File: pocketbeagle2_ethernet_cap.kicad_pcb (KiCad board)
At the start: 4 copper layers, 35.3 x 55.3 mm, 84 parts, among them J1 RJ45_1840888-1, J2 Header_18x02_2.54mm_2.54mm_St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, J3 Header_18x02_2.54mm_2.54mm_St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, Q1 BSS138LT1G, Q2 BSS138LT1G, Q3 BSS138LT1G, U1 PocketBeagle2, U2 DP83867IRPAPR, U3 TPS7A2011PDBVR, U4 TPS7A2025PDBVR, Y1 25M

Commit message: Switch BOM to in-stock LCSC parts, U3 to TLV73311
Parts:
- U3: value TPS7A2011PDBVR -> TLV73311PDBVR
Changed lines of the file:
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@@
 			)
 		)
-		(property "Value" "TPS7A2011PDBVR"
+		(property "Value" "TLV73311PDBVR"
 			(at 0 2.4 0)
 			(unlocked yes)

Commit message: Move LED drivers, pull-ups, TD0/TD2 resistors to top side
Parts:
- Q1, Q2, Q3, R10, R20, R21, R24, R31, R32, R8: moved to F.Cu
- moved Q1 14.2 mm to (202.2, 62.3)
- moved Q2 7.94 mm to (198.7, 62.3)
- moved Q3 4.77 mm to (195.2, 62.3)
- moved R24 3.63 mm to (190.3, 65.3), turned to 180 degrees
- moved R31 2.53 mm to (188.0, 91.2)
- moved R8 2.41 mm to (190.3, 63.9)
- moved R32 2.00 mm to (188.0, 90.0), turned to 0 degrees
- moved R10 0.90 mm to (205.2, 70.0)
- moved R20 0.80 mm to (205.2, 61.1)
- moved R21 0.80 mm to (205.2, 63.7)
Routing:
- net Net-(D1-K): track 2.63 -> 21.6 mm, vias 1 -> 2
- net /network/phy/LED0_PHY_to_Q1: track 59.5 -> 71.4 mm
- net Net-(D2-K): track 2.55 -> 13.3 mm, vias 1 -> 2
- net /VDD_3V3: track 178.7 -> 187.9 mm, vias 10 -> 11
- net /network/phy/LED1_PHY_to_Q2: track 55.7 -> 61.4 mm, vias 1 -> 2
- net Net-(U2-TX_D0): track 65.6 -> 60.1 mm, vias 1 -> 2
- net /INT_PWDN_N_CPU_PHY: track 27.2 -> 30.7 mm, vias 0 -> 1
- net /RGMII_TD0_CPU_to_PHY: track 2.26 -> 4.78 mm, vias 0 -> 1
- net GND: track 53.8 -> 56.3 mm, vias 101 -> 96
- net Net-(D3-K): track 2.55 -> 5.02 mm, vias 1 -> 2
- net Net-(U2-TX_D2): track 73.5 -> 71.2 mm, vias 1 -> 2
- net /network/phy/LED2_PHY_to_Q3: track 54.2 -> 52.8 mm, vias 1 -> 2
- net /RGMII_TD2_CPU_to_PHY: track 4.45 -> 5.35 mm
- net /MDIO_MDC_CPU_PHY: track 42.1 -> 42.9 mm
- net /MDIO_DIO_CPU_PHY: track 36.1 -> 36.9 mm

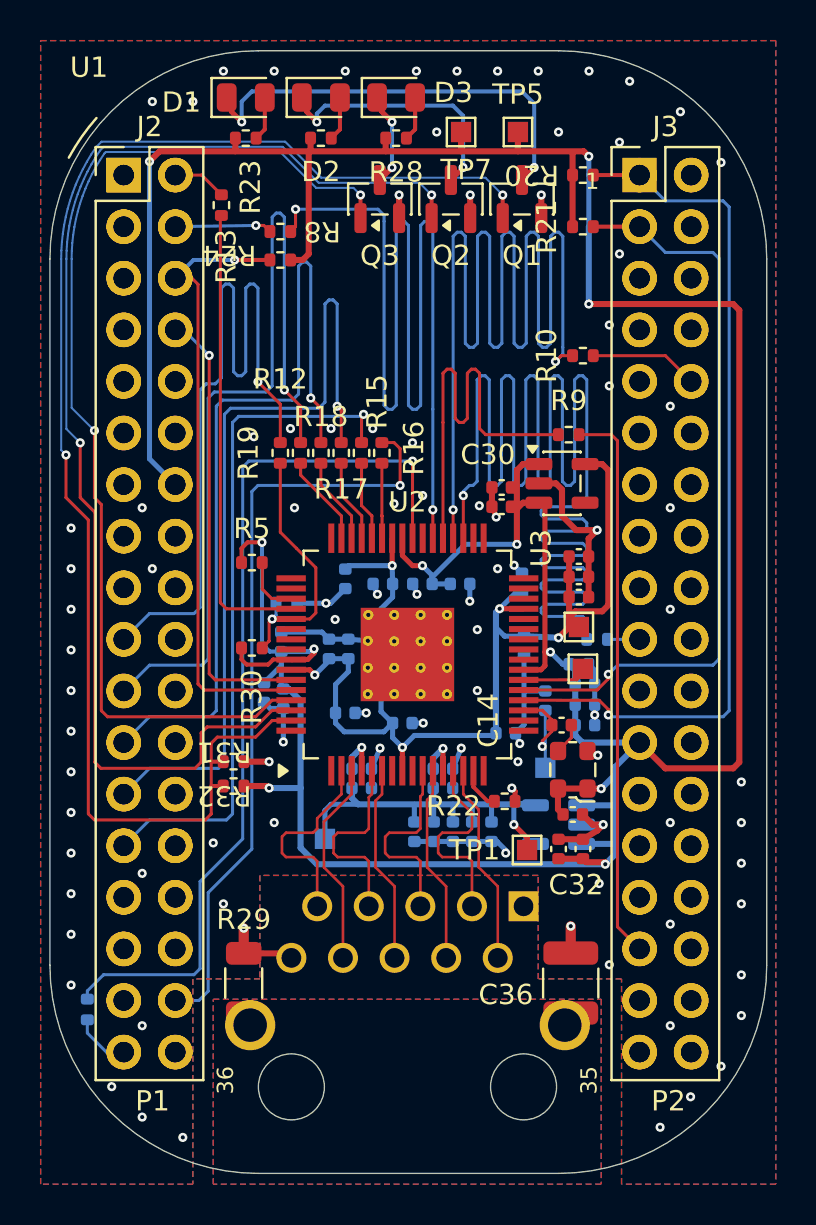
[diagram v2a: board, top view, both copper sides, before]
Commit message: Move LDO, decoupling and series resistors to top side
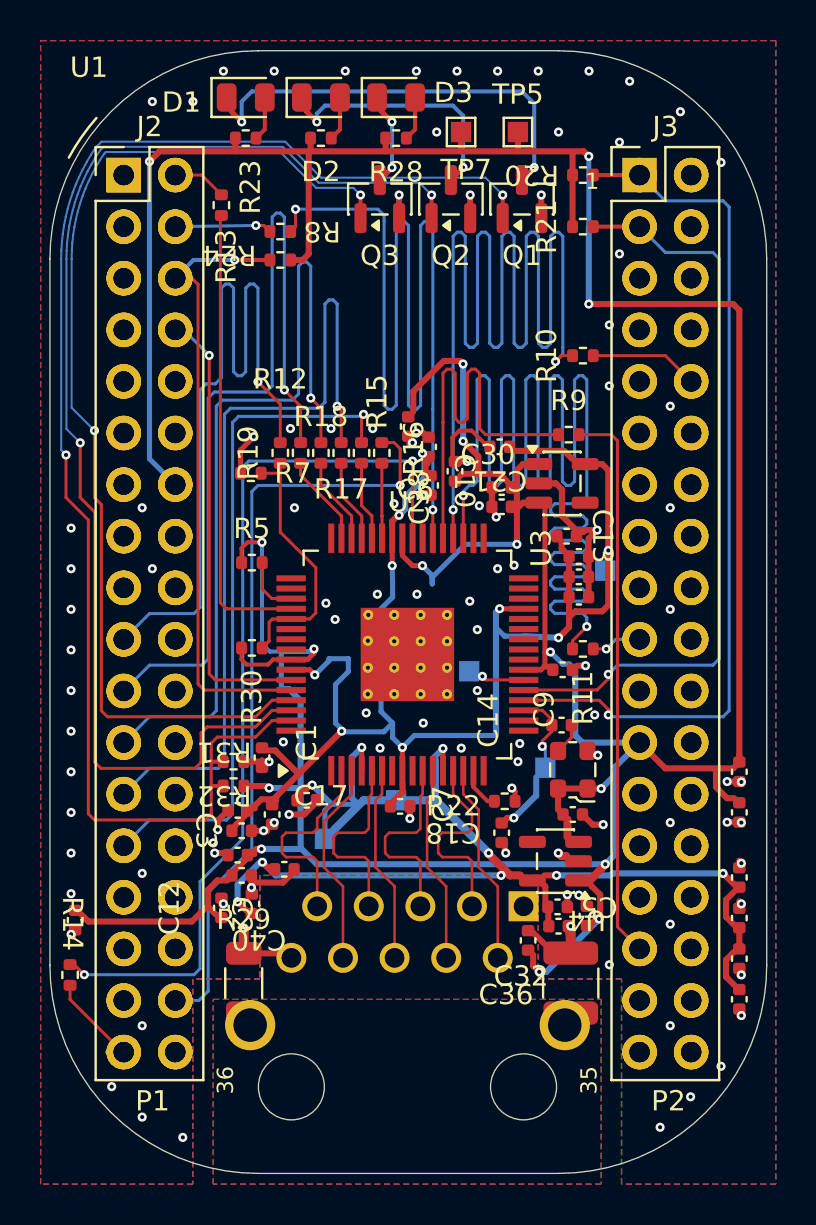
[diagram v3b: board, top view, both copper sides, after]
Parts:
- C1, C10, C11, C12, C13, C15, C16, C17, C18, C19, C2, C20, C21, C22, C23, C24, C25, C3, C33, C37, C38, C39, C40, C5, C6, C7, C8, C9, R11, R14, R7, U4: moved to F.Cu
- TP1, TP2, TP8: moved to B.Cu
- moved C22 27.7 mm to (180.2, 97.8), turned to -90 degrees
- moved C11 16.2 mm to (212.9, 95.7), turned to 90 degrees
- moved C8 15.6 mm to (212.9, 97.7), turned to 90 degrees
- moved C15 15.5 mm to (212.9, 101.7)
- moved C19 15.4 mm to (212.9, 99.7)
- moved C23 12.1 mm to (189.4, 89.8), turned to -90 degrees
- moved C2 11.7 mm to (188.4, 95.6), turned to 0 degrees
- moved C40 11.0 mm to (188.9, 97.0), turned to 90 degrees
- moved C12 10.7 mm to (187.4, 97.2), turned to 90 degrees
- moved C3 9.93 mm to (188.4, 93.4), turned to 0 degrees
- moved C21 9.87 mm to (201.1, 74.5), turned to 180 degrees
- moved C25 9.64 mm to (188.2, 92.4), turned to 180 degrees
- moved C5 8.83 mm to (203.9, 97.2)
- moved C20 8.73 mm to (212.9, 92.5), turned to -90 degrees
- moved C16 8.29 mm to (212.9, 90.5), turned to -90 degrees
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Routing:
- net /VDD_3V3: track 187.9 -> 216.4 mm, vias 11 -> 16
- net /VDD_2V5: track 28.4 -> 55.5 mm, vias 3 -> 9
- net GND: track 56.3 -> 37.8 mm, vias 96 -> 107
- net /VDD_1V1: track 55.8 -> 72.3 mm, vias 5 -> 10
- net Net-(U2-TX_D3): track 88.0 -> 84.0 mm, vias 1 -> 2
- net /RGMII_TX_CLK_CPU_to_PHY: track 2.83 -> 5.26 mm
- net /network/oscillator/CLK_25M_OSC_to_PHY: track 6.03 -> 7.21 mm, vias 1 -> 2
- net /RGMII_TD3_CPU_to_PHY: track 1.58 -> 2.47 mm, vias 0 -> 1
- net Net-(U2-GTX_CLK): track 44.2 -> 44.6 mm, vias 1 -> 2
- net Net-(U2-CLK_OUT): track 3.04 -> 2.80 mm, vias 0 -> 1
- net /network/phy/STRAP_RX_CTRL_PHY: track 12.8 -> 12.9 mm, vias 1 -> 0

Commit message: Silkscreen re-placed, 0402 3D models, orphan via removed
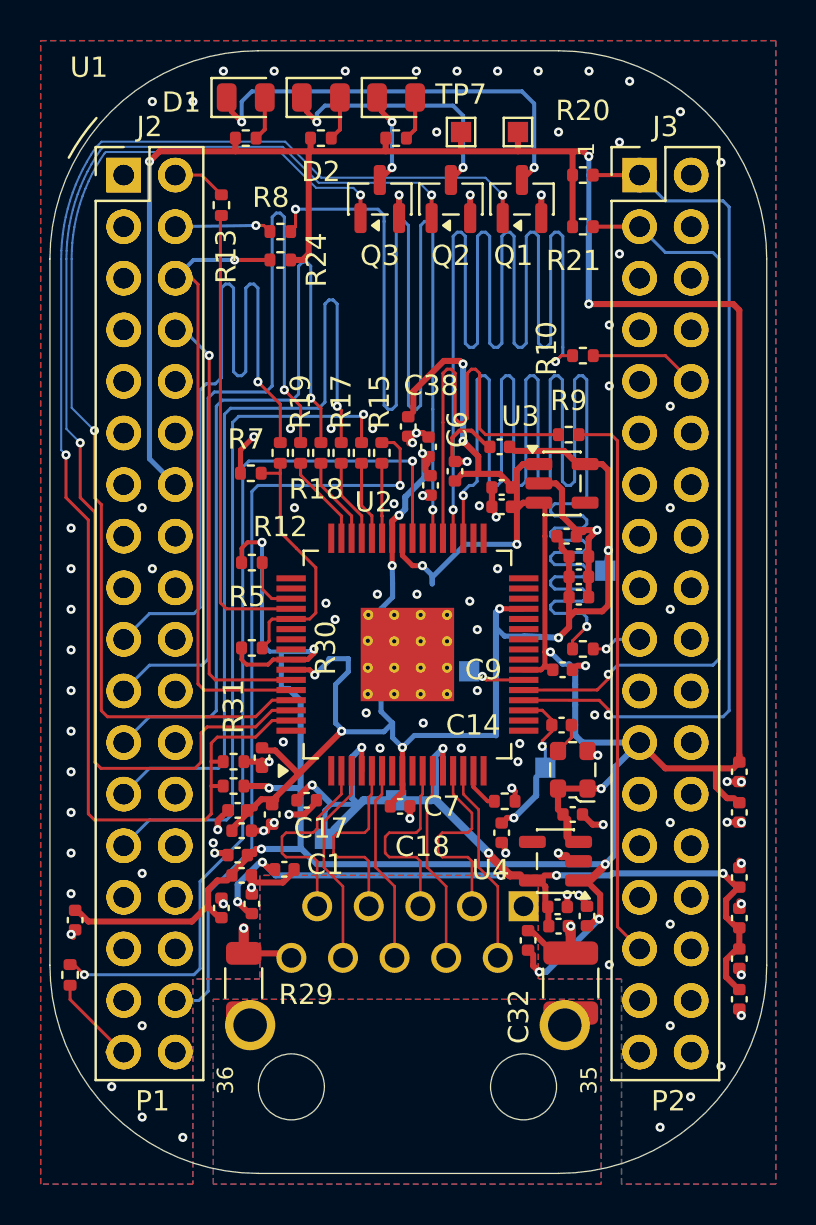
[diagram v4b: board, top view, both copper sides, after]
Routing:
- net /VDD_1V1: vias 10 -> 9
